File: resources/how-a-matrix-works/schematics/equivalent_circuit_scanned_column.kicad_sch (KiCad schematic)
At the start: 10 parts

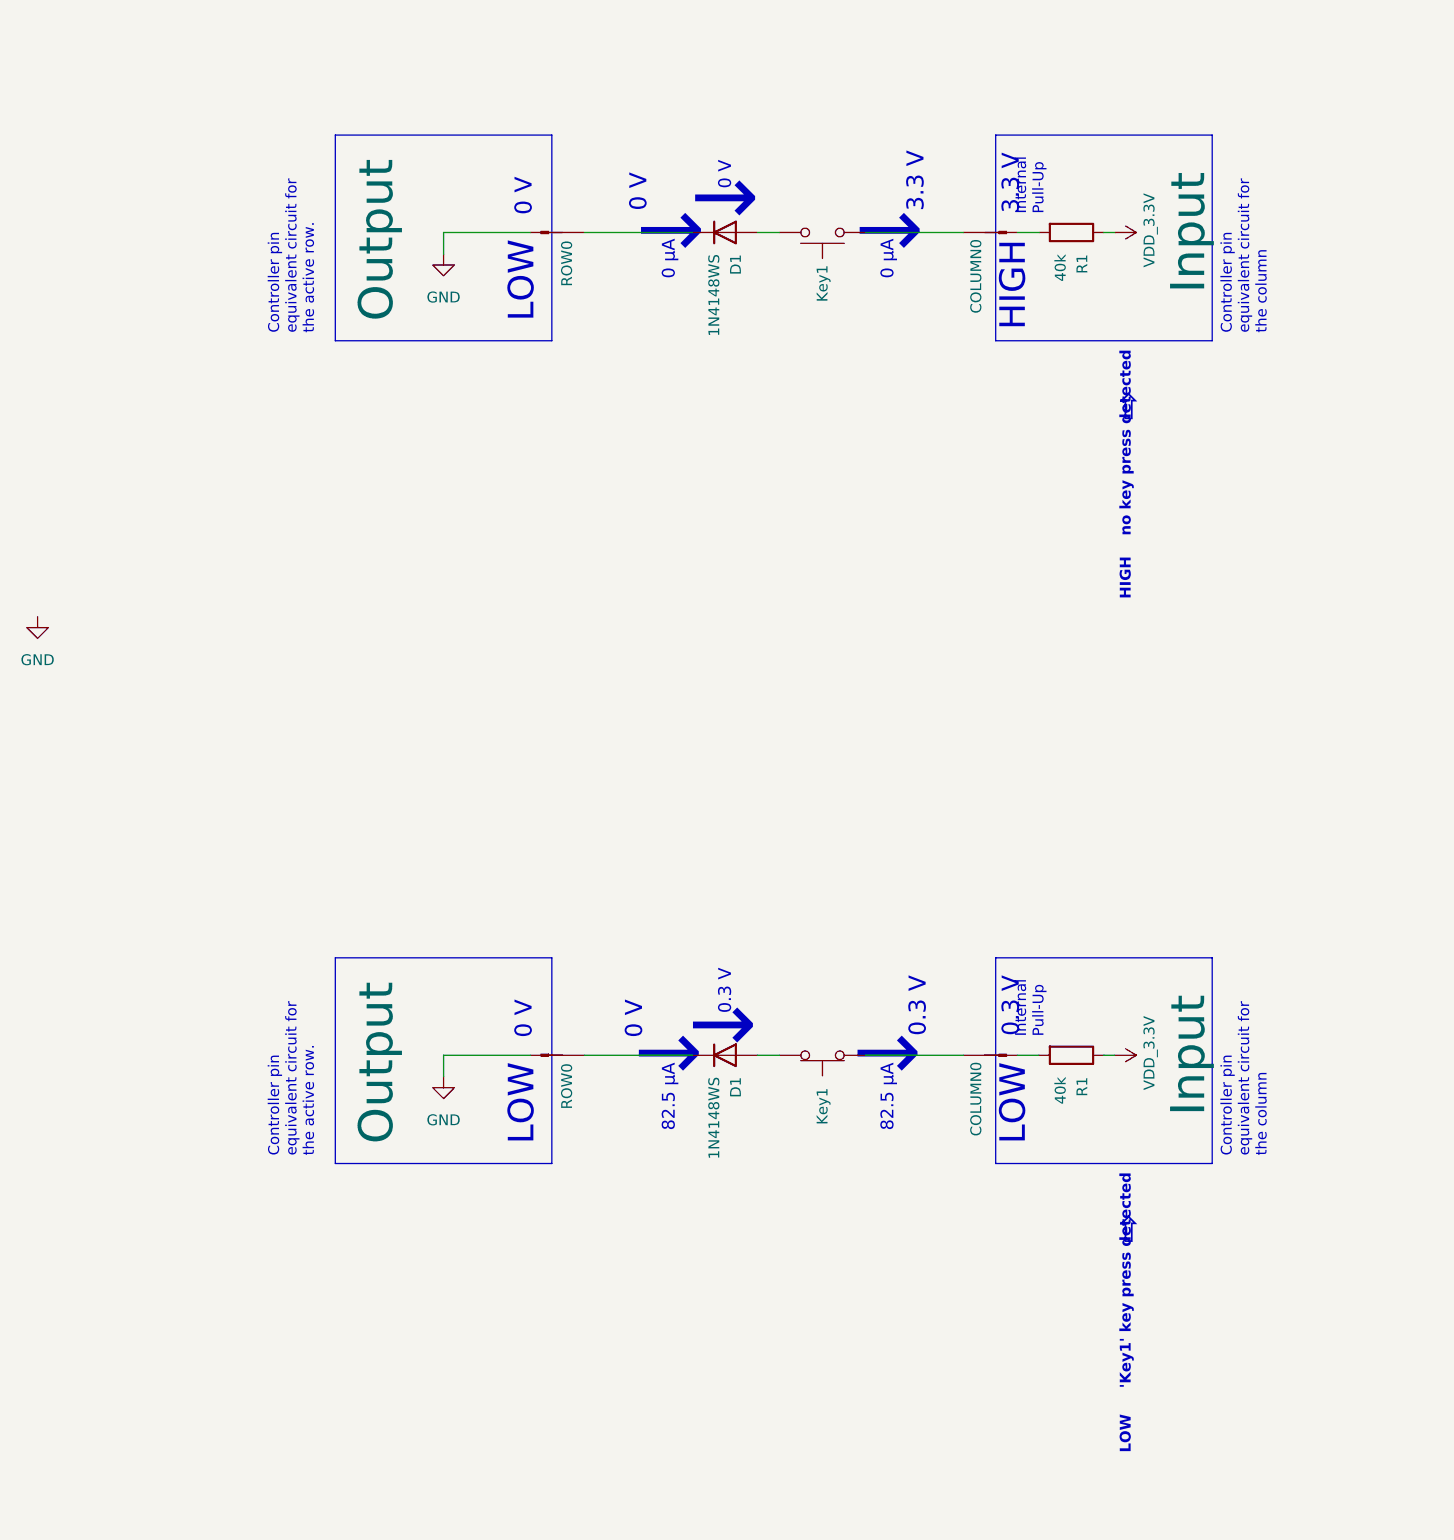
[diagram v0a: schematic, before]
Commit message: add equivalent circuit images
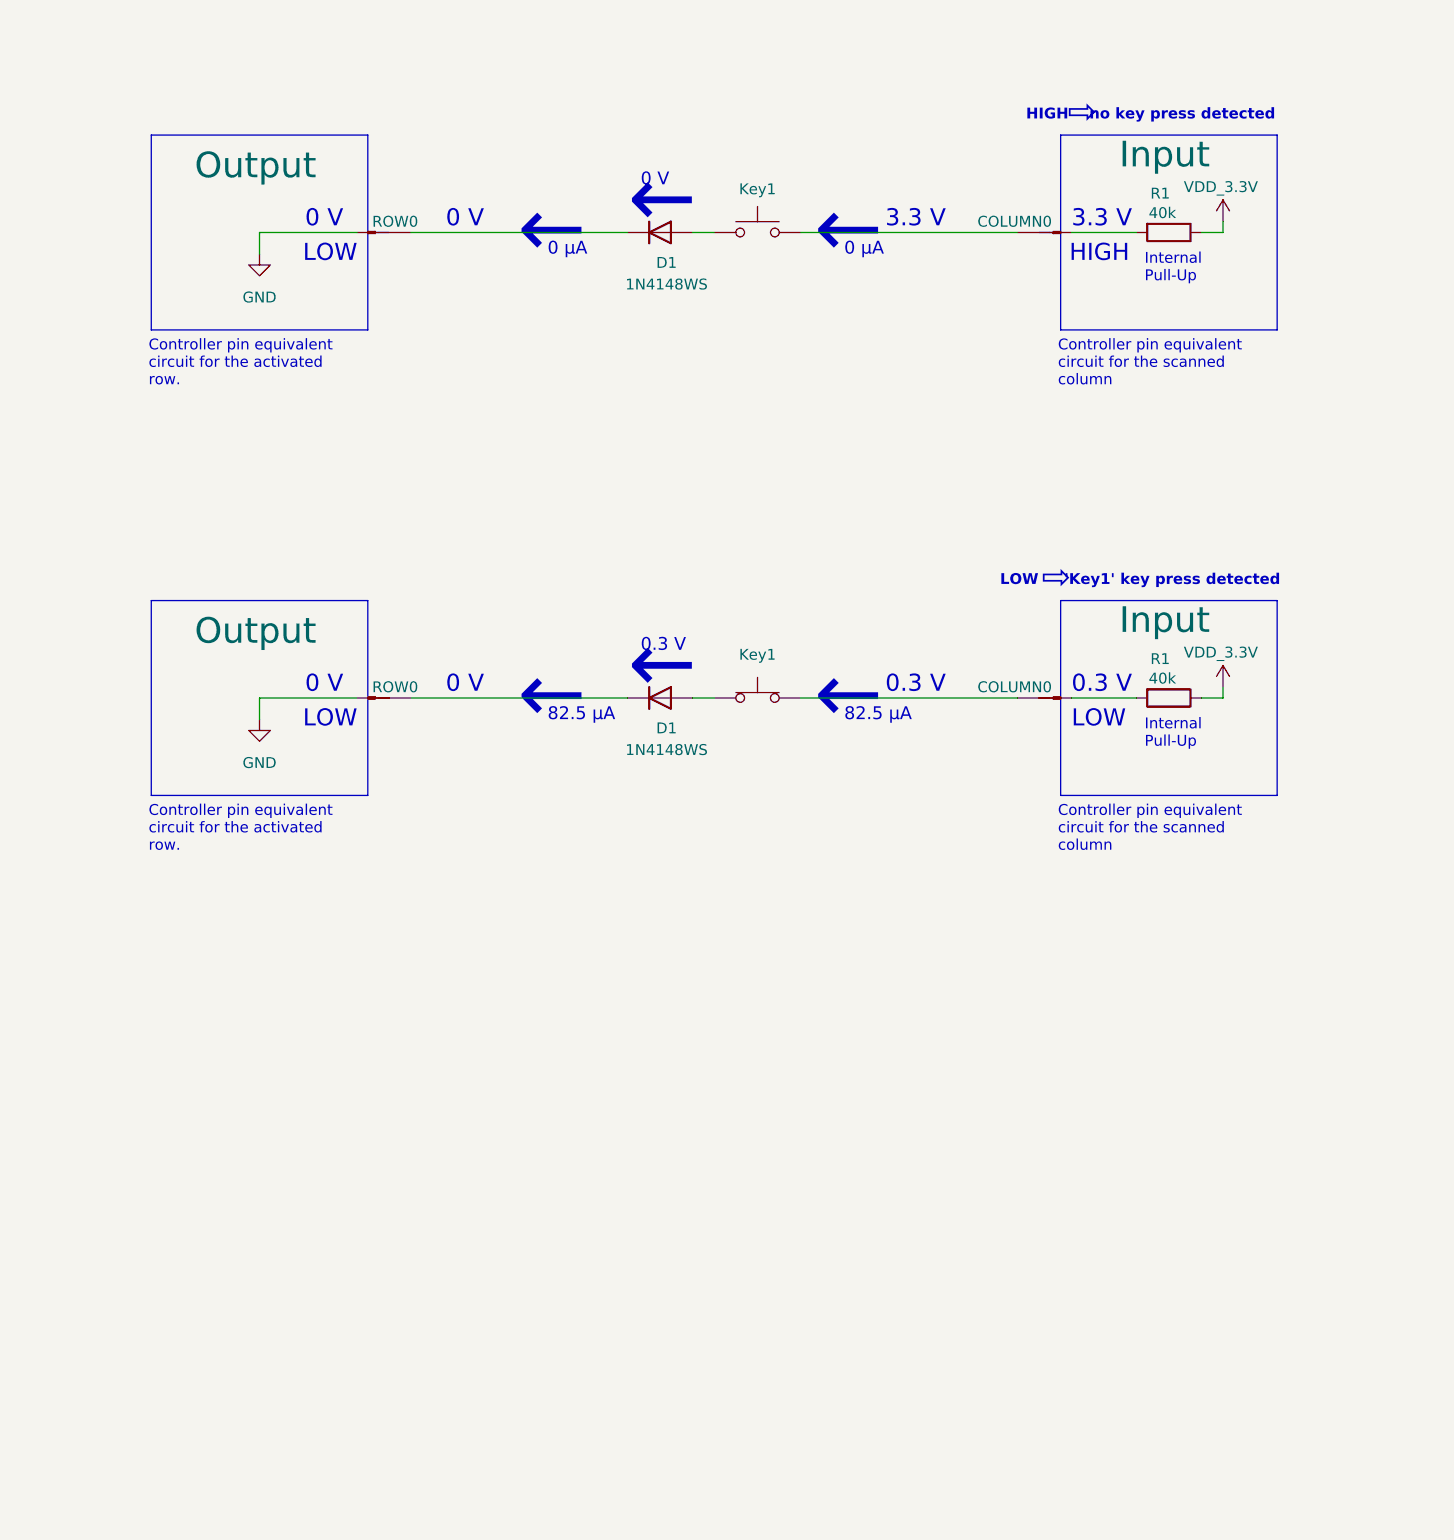
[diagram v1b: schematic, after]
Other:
- note added: "←"
- note removed: "↓"
- moved on the sheet: D1, Input, Key1, Output, R1

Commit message: update equivalent circuit schematic and images
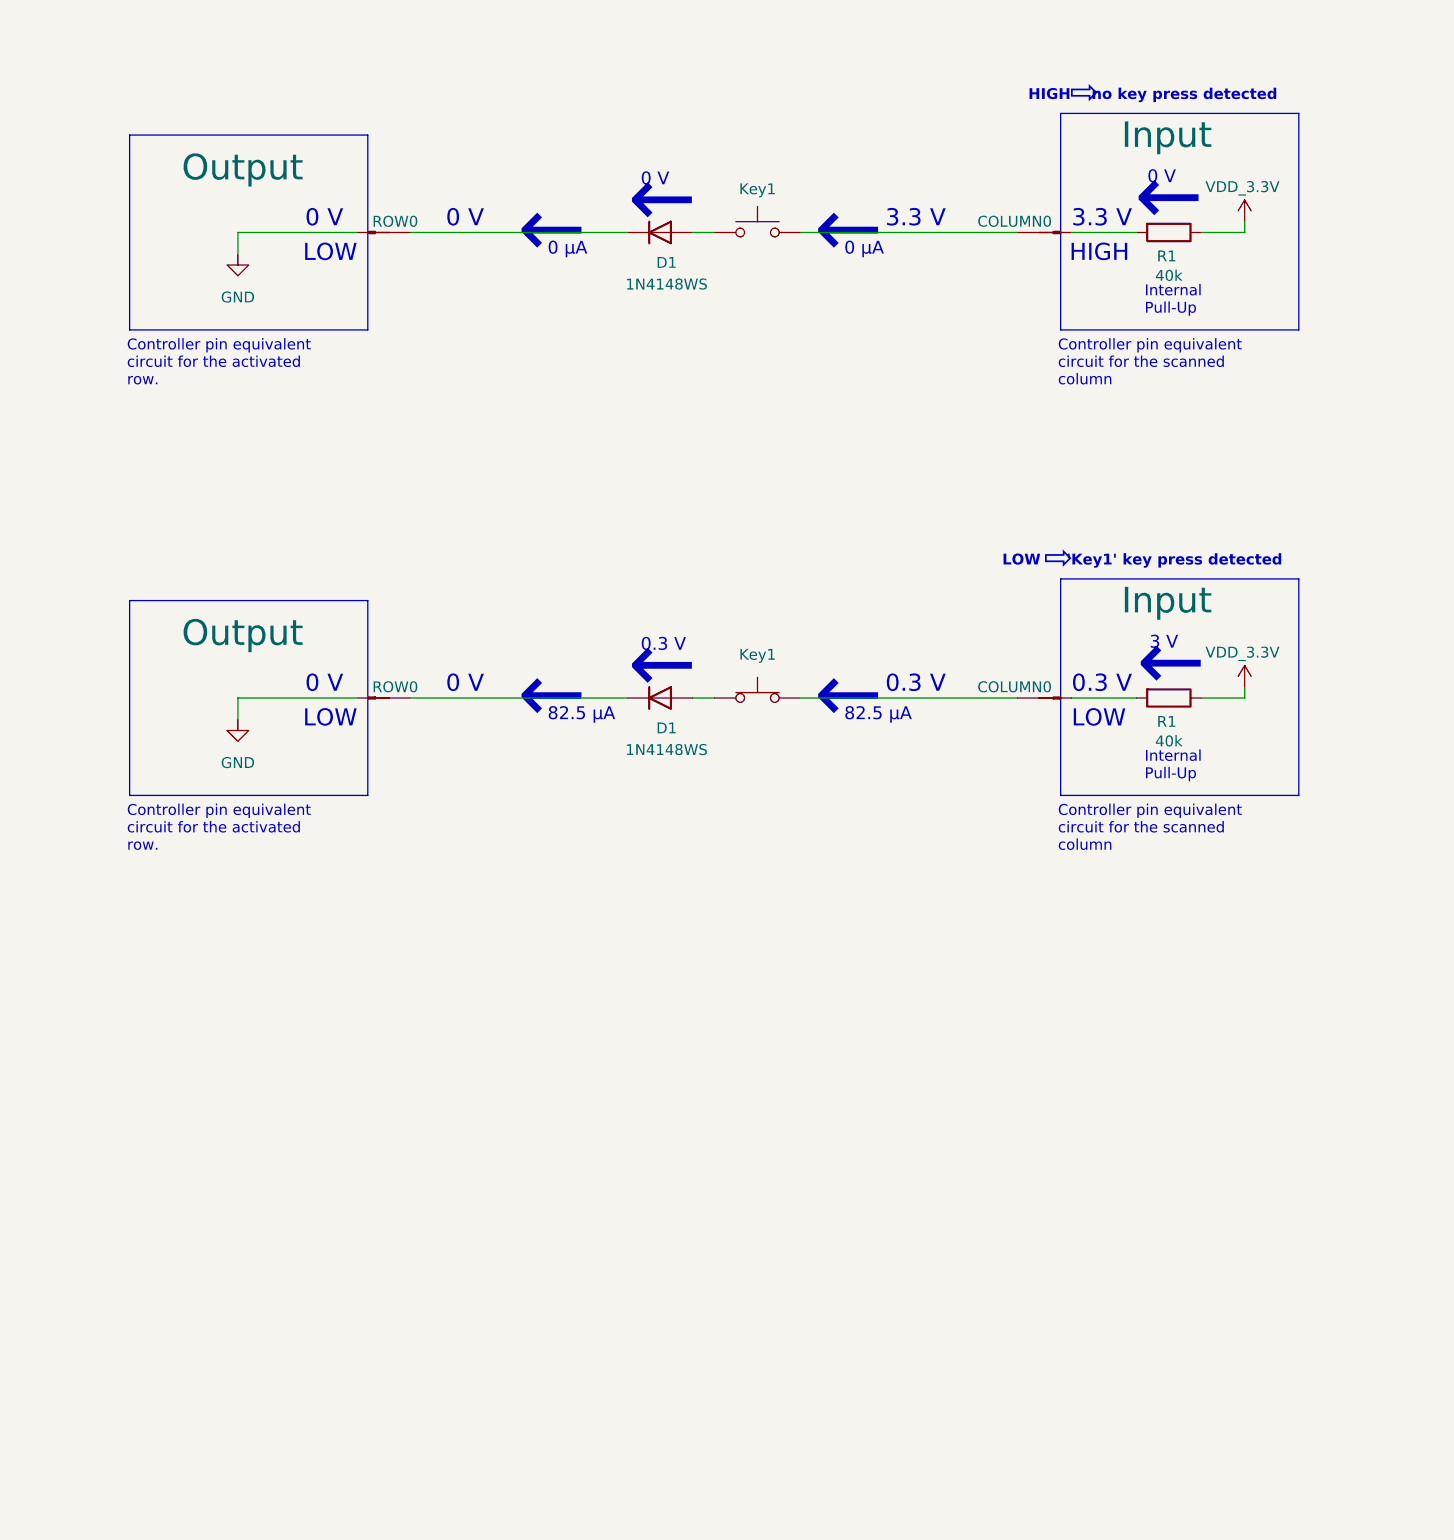
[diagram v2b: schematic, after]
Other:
- note added: "3 V"

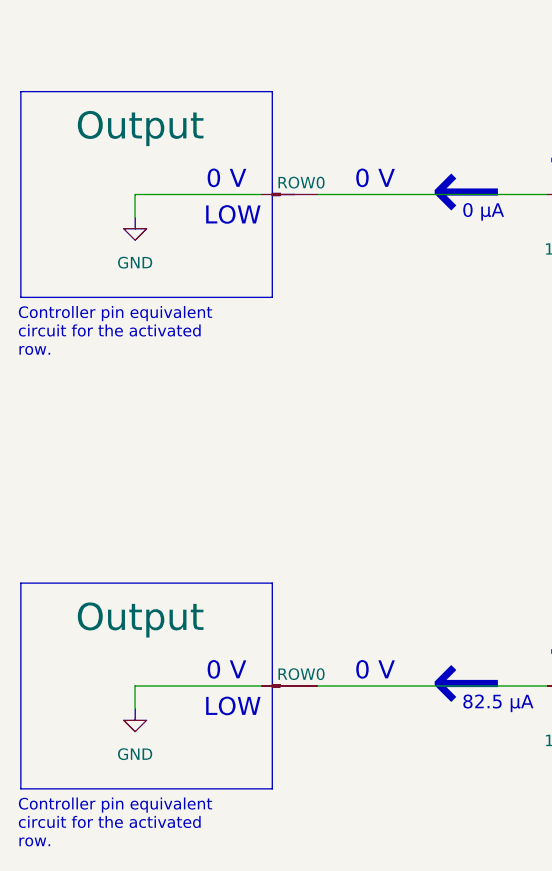
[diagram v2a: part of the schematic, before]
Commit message: update equivalent circuit schematic and images
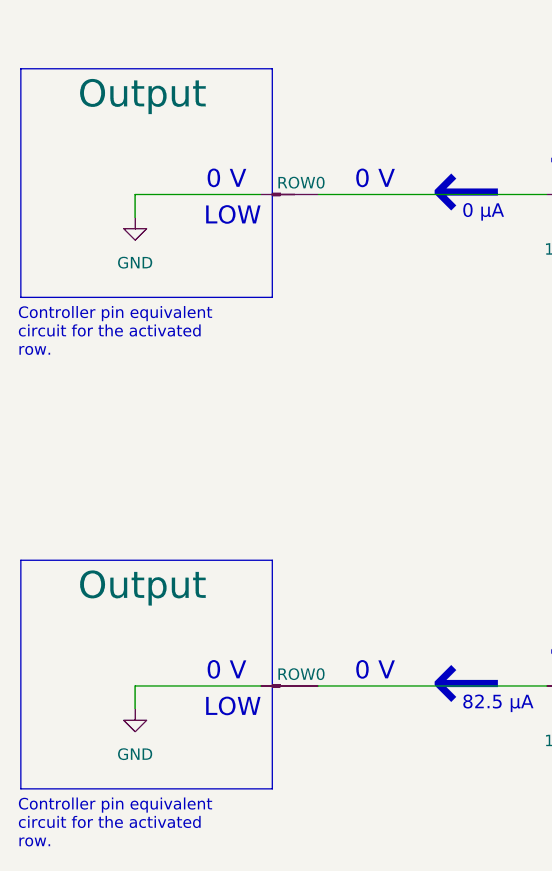
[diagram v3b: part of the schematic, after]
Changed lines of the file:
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@@
 	)
 	(rectangle
-		(start 105.41 39.37)
+		(start 105.41 36.83)
 		(end 133.35 62.23)
 		(stroke
@@
 	)
 	(rectangle
-		(start 105.41 93.98)
+		(start 105.41 91.44)
 		(end 133.35 116.84)
 		(stroke
@@
 		(dnp no)
 		(property "Reference" "Output"
-			(at 111.506 97.79 0)
+			(at 111.76 94.234 0)
 			(effects
 				(font
@@
 		(dnp no)
 		(property "Reference" "Output"
-			(at 111.506 43.18 0)
-			(effects
-				(font
+			(at 111.76 39.624 0)
+			(effects
+				(font
